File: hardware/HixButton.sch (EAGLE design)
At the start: 28 parts, among them J1 FTDIFTDI_ANGLED, U1 ESP8266(ESP12E)V2, U2 TPS3839L30, U3 CN3058E, U4 WS2812

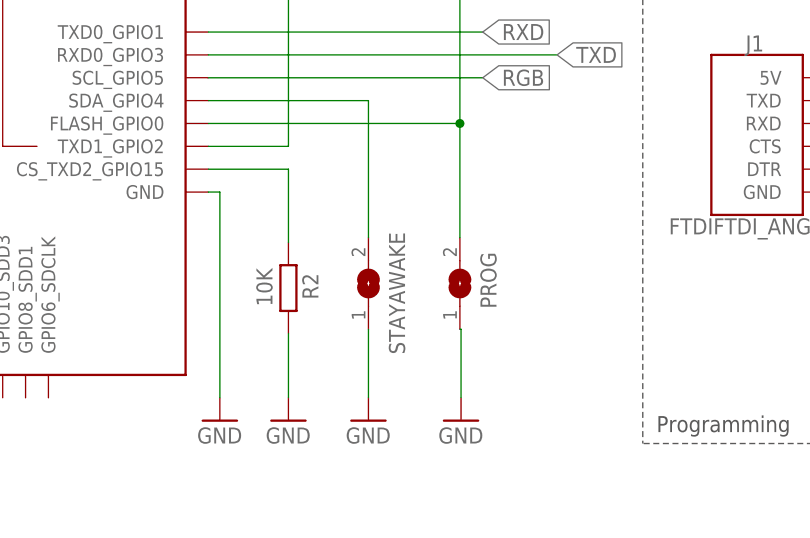
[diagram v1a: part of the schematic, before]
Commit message: added sj 3d model
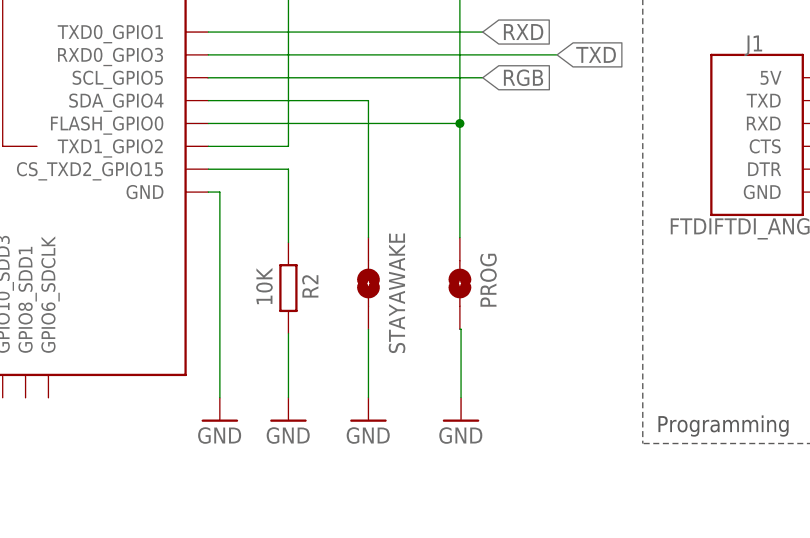
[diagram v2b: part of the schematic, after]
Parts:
- PROG: device jumper:SJ -> 0_HixField:SJ; SPICEPREFIX (none) -> B
- STAYAWAKE: device jumper:SJ -> 0_HixField:SJ
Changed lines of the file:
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@@
 <part name="R1" library="rcl" library_urn="urn:adsk.eagle:library:334" deviceset="R-EU_" device="R1206" package3d_urn="urn:adsk.eagle:package:23540/2" value="10K"/>
 <part name="SUPPLY4" library="0_HixField" library_urn="urn:adsk.eagle:library:13392178" deviceset="3.3V" device=""/>
-<part name="STAYAWAKE" library="jumper" library_urn="urn:adsk.eagle:library:252" deviceset="SJ" device="" package3d_urn="urn:adsk.eagle:package:15471/1"/>
+<part name="STAYAWAKE" library="0_HixField" library_urn="urn:adsk.eagle:library:13392178" deviceset="SJ" device="" package3d_urn="urn:adsk.eagle:package:25478059/2"/>
 <part name="GND2" library="supply1" library_urn="urn:adsk.eagle:library:371" deviceset="GND" device=""/>
 <part name="LIFEPO4" library="0_HixField" library_urn="urn:adsk.eagle:library:13392178" deviceset="XH2P" device="" package3d_urn="urn:adsk.eagle:package:12836045/3"/>
@@
 <part name="R4" library="rcl" library_urn="urn:adsk.eagle:library:334" deviceset="R-EU_" device="R1206" package3d_urn="urn:adsk.eagle:package:23540/2" value="330"/>
 <part name="GND8" library="supply1" library_urn="urn:adsk.eagle:library:371" deviceset="GND" device=""/>
-<part name="PROG" library="jumper" library_urn="urn:adsk.eagle:library:252" deviceset="SJ" device="" package3d_urn="urn:adsk.eagle:package:15471/1"/>
+<part name="PROG" library="0_HixField" library_urn="urn:adsk.eagle:library:13392178" deviceset="SJ" device="" package3d_urn="urn:adsk.eagle:package:25478059/2">
+<attribute name="SPICEPREFIX" value="B"/>
+</part>
 <part name="C2" library="rcl" library_urn="urn:adsk.eagle:library:334" deviceset="C-EU" device="C1206" package3d_urn="urn:adsk.eagle:package:23618/2" value="100nF"/>
 <part name="C3" library="rcl" library_urn="urn:adsk.eagle:library:334" deviceset="C-EU" device="C1206" package3d_urn="urn:adsk.eagle:package:23618/2" value="100nF">
